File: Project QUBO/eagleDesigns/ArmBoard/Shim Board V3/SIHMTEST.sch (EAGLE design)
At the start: 30 parts, among them IC1 MCP2551/SN, U1 BME280

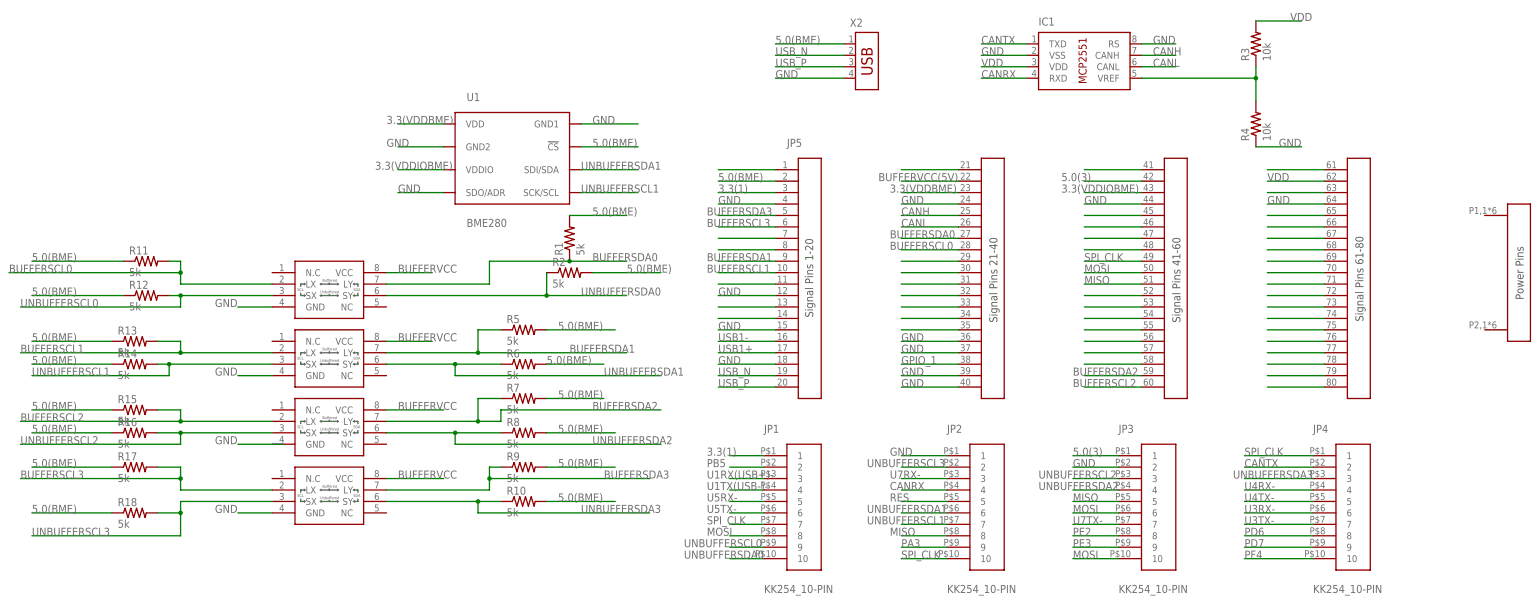
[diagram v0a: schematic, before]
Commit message: 
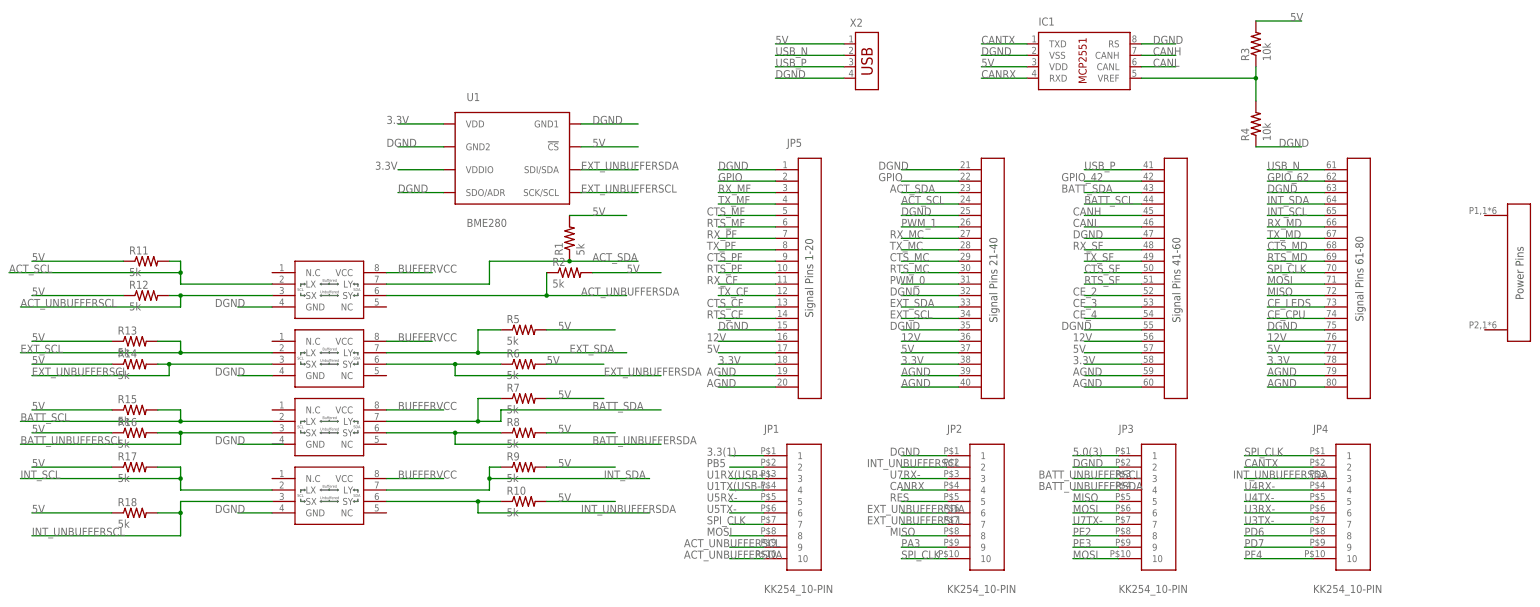
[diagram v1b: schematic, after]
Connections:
- net N$11 renamed RX_CF
- net N$13 renamed CTS_CF
- net N$14 renamed RTS_CF
- net N$29 renamed CTS_MC
- net N$30 renamed RTS_MC
- net N$31 renamed PWM_0
- net N$48 renamed RX_SF
- net N$52 renamed CE_2
- net N$53 renamed CE_3
- net N$54 renamed CE_4
- net N$66 renamed RX_MD
- net N$67 renamed TX_MD
- net N$68 renamed CTS_MD
- net N$69 renamed RTS_MD
- net N$7 renamed RX_PF
- net N$73 renamed CE_LEDS
- net N$74 renamed CE_CPU
- net N$8 renamed TX_PF
- net UNBUFFERSCL0 renamed ACT_UNBUFFERSCL
- net UNBUFFERSCL1 renamed EXT_UNBUFFERSCL
- net UNBUFFERSCL2 renamed BATT_UNBUFFERSCL
- net UNBUFFERSCL3 renamed INT_UNBUFFERSCL
- net UNBUFFERSDA0 renamed ACT_UNBUFFERSDA
- net UNBUFFERSDA1 renamed EXT_UNBUFFERSDA
- net UNBUFFERSDA2 renamed BATT_UNBUFFERSDA
- net UNBUFFERSDA3 renamed INT_UNBUFFERSDA
- removed net 3.3(VDDBME): JP5.P$23, U1.VDD
- removed net 3.3(VDDIOBME): JP5.P$43, U1.VDDIO
- removed net 5.0(BME): JP5.P$2, R1.2, R10.2, R11.1, R12.1, R13.1, R14.1, R15.1, R16.1, R17.1, R18.1, R2.2, R5.2, R6.2, R7.2, R8.2, R9.2, U1.!CS, X2.1
- removed net BUFFERSCL0: JP5.P$28, R11.2, U$1.LX
- removed net BUFFERSCL1: JP5.P$10, R13.2, U$2.LX
- removed net BUFFERSCL2: JP5.P$60, R15.2, U$3.LX
- removed net BUFFERSCL3: JP5.P$6, R17.2, U$4.LX
- removed net BUFFERSDA0: JP5.P$27, R1.1, U$1.LY
- removed net BUFFERSDA1: JP5.P$9, R5.1, U$2.LY
- removed net BUFFERSDA2: JP5.P$59, R7.1, U$3.LY
- removed net BUFFERSDA3: JP5.P$5, R9.1, U$4.LY
- removed net BUFFERVCC(5V): JP5.P$22
- removed net GND: IC1.RS, IC1.VSS, JP2.1, JP3.2, JP5.P$12, JP5.P$15, JP5.P$18, JP5.P$24, JP5.P$36, JP5.P$37, JP5.P$39, JP5.P$4, JP5.P$40, JP5.P$44, JP5.P$64, R4.1, U$1.GND, U$2.GND, U$4.GND, U1.GND1, U1.GND2, U1.SDO/ADR, X2.4
- removed net GPIO_1: JP5.P$38
- removed net N$1: JP5.P$1
- removed net N$21: JP5.P$21
- removed net N$32: JP5.P$32
- removed net N$33: JP5.P$33
- removed net N$34: JP5.P$34
- removed net N$35: JP5.P$35
- removed net N$41: JP5.P$41
- removed net N$45: JP5.P$45
- removed net N$46: JP5.P$46
- removed net N$47: JP5.P$47
- removed net N$55: JP5.P$55
- removed net N$56: JP5.P$56
- removed net N$57: JP5.P$57
- removed net N$58: JP5.P$58
- removed net N$61: JP5.P$61
- removed net N$63: JP5.P$63
- removed net N$65: JP5.P$65
- removed net N$70: JP5.P$70
- removed net N$71: JP5.P$71
- removed net N$72: JP5.P$72
- removed net N$75: JP5.P$75
- removed net N$76: JP5.P$76
- removed net N$77: JP5.P$77
- removed net N$78: JP5.P$78
- removed net N$79: JP5.P$79
- removed net N$80: JP5.P$80
- removed net USB1+: JP5.P$17
- removed net USB1-: JP5.P$16
- removed net VDD: IC1.VDD, JP5.P$62, R3.2
- new net 12V: JP5.P$16, JP5.P$36, JP5.P$56, JP5.P$76
- new net 3.3V: JP5.P$18, JP5.P$38, JP5.P$58, JP5.P$78, U1.VDD, U1.VDDIO
- new net 5V: IC1.VDD, JP5.P$17, JP5.P$37, JP5.P$57, JP5.P$77, R1.2, R10.2, R11.1, R12.1, R13.1, R14.1, R15.1, R16.1, R17.1, R18.1, R2.2, R3.2, R5.2, R6.2, R7.2, R8.2, R9.2, U1.!CS, X2.1
- new net ACT_SCL: JP5.P$24, R11.2, U$1.LX
- new net ACT_SDA: JP5.P$23, R1.1, U$1.LY
- new net AGND: JP5.P$19, JP5.P$20, JP5.P$39, JP5.P$40, JP5.P$59, JP5.P$60, JP5.P$79, JP5.P$80
- new net BATT_SCL: JP5.P$44, R15.2, U$3.LX
- new net BATT_SDA: JP5.P$43, R7.1, U$3.LY
- new net CTS_MF: JP5.P$5
- new net CTS_PF: JP5.P$9
- new net CTS_SF: JP5.P$50
- new net DGND: IC1.RS, IC1.VSS, JP2.1, JP3.2, JP5.P$1, JP5.P$15, JP5.P$21, JP5.P$25, JP5.P$32, JP5.P$35, JP5.P$47, JP5.P$55, JP5.P$63, JP5.P$75, R4.1, U$1.GND, U$2.GND, U$4.GND, U1.GND1, U1.GND2, U1.SDO/ADR, X2.4
- new net EXT_SCL: JP5.P$34, R13.2, U$2.LX
- new net EXT_SDA: JP5.P$33, R5.1, U$2.LY
- new net GPIO: JP5.P$2, JP5.P$22
- new net GPIO_42: JP5.P$42
- new net GPIO_62: JP5.P$62
- new net INT_SCL: JP5.P$65, R17.2, U$4.LX
- new net INT_SDA: JP5.P$64, R9.1, U$4.LY
- new net PWM_1: JP5.P$26
- new net RTS_MF: JP5.P$6
- new net RTS_PF: JP5.P$10
- new net RTS_SF: JP5.P$51
- new net RX_MC: JP5.P$27
- new net RX_MF: JP5.P$3
- new net TX_CF: JP5.P$12
- new net TX_MC: JP5.P$28
- new net TX_MF: JP5.P$4
- new net TX_SF: JP5.P$49
- net 3.3(1): no longer JP5.P$3
- net 5.0(3): no longer JP5.P$42
- net CANH: now also JP5.P$45; no longer JP5.P$25
- net CANL: now also JP5.P$46; no longer JP5.P$26
- net MISO: now also JP5.P$72; no longer JP5.P$51
- net MOSI: now also JP5.P$71; no longer JP5.P$50
- net SPI_CLK: now also JP5.P$70; no longer JP5.P$49
- net USB_N: now also JP5.P$61; no longer JP5.P$19
- net USB_P: now also JP5.P$41; no longer JP5.P$20

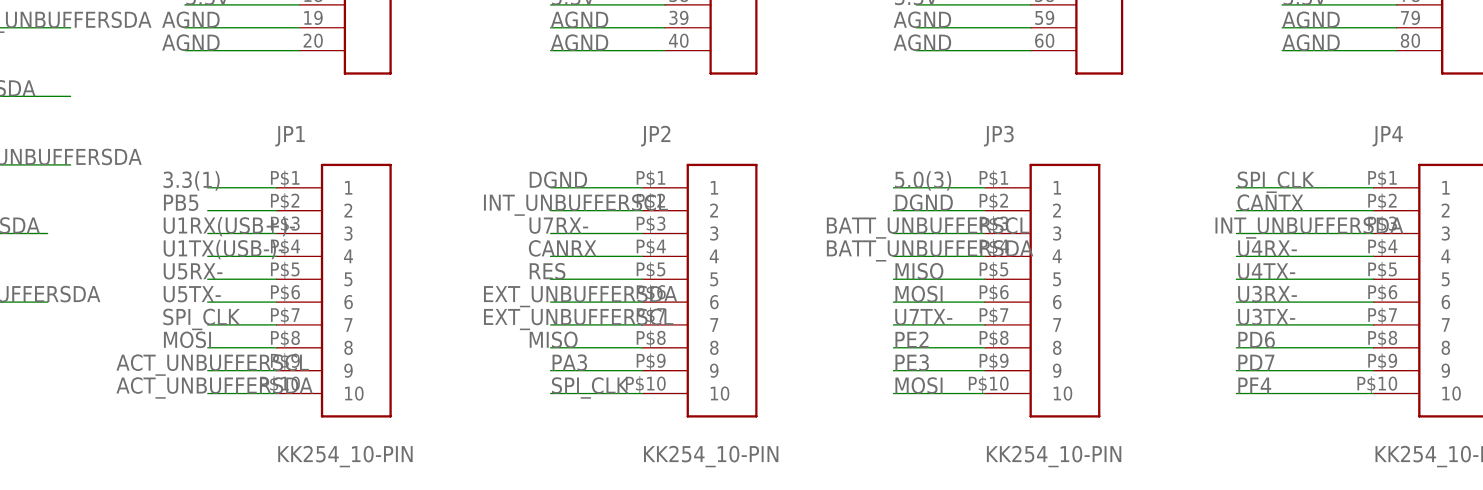
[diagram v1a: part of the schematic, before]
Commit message: 
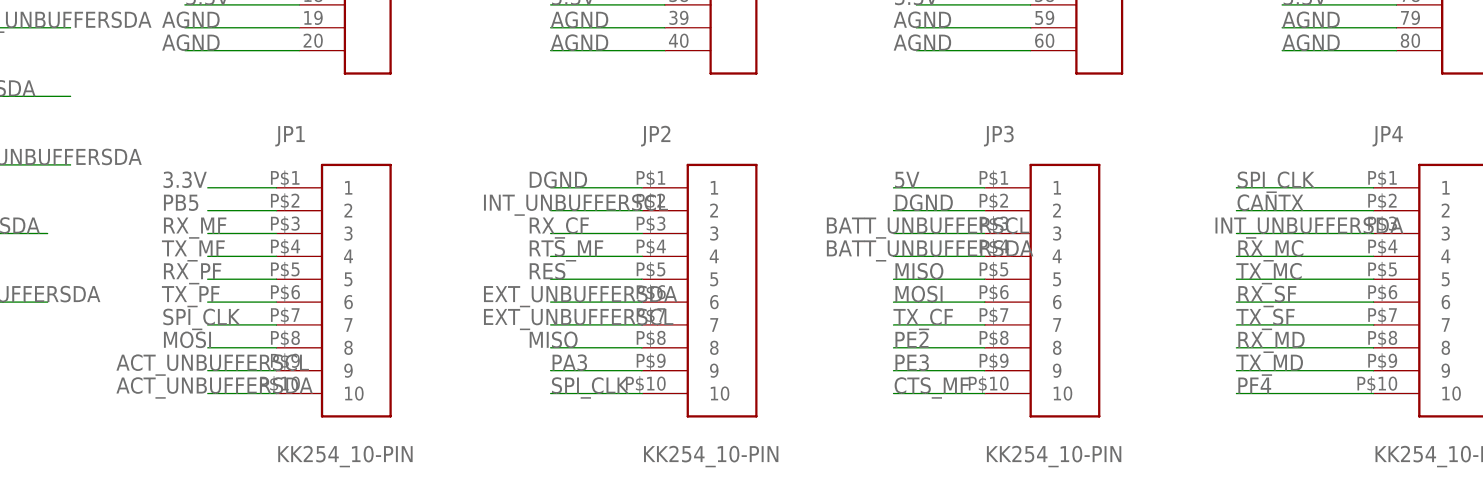
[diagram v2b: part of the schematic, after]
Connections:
- removed net 3.3(1): JP1.1
- removed net 5.0(3): JP3.1
- removed net PD6: JP4.8
- removed net PD7: JP4.9
- removed net U1RX(USB+)-: JP1.3
- removed net U1TX(USB-)-: JP1.4
- removed net U3RX-: JP4.6
- removed net U3TX-: JP4.7
- removed net U4RX-: JP4.4
- removed net U4TX-: JP4.5
- removed net U5RX-: JP1.5
- removed net U5TX-: JP1.6
- removed net U7RX-: JP2.3
- removed net U7TX-: JP3.7
- net 3.3V: now also JP1.1
- net 5V: now also JP3.1
- net CANRX: no longer JP2.4
- net CTS_MF: now also JP3.10
- net MOSI: no longer JP3.10
- net RTS_MF: now also JP2.4
- net RX_CF: now also JP2.3
- net RX_MC: now also JP4.4
- net RX_MD: now also JP4.8
- net RX_MF: now also JP1.3
- net RX_PF: now also JP1.5
- net RX_SF: now also JP4.6
- net TX_CF: now also JP3.7
- net TX_MC: now also JP4.5
- net TX_MD: now also JP4.9
- net TX_MF: now also JP1.4
- net TX_PF: now also JP1.6
- net TX_SF: now also JP4.7
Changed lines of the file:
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@@
 <?xml version="1.0" encoding="utf-8"?>
 <!DOCTYPE eagle SYSTEM "eagle.dtd">
-<eagle version="7.6.0">
+<eagle version="8.0.0">
 <drawing>
 <settings>
@@
 </segment>
 </net>
-<net name="3.3(1)" class="0">
-<segment>
-<pinref part="JP1" gate="G$1" pin="1"/>
-<wire x1="10.16" y1="88.9" x2="2.54" y2="88.9" width="0.1524" layer="91"/>
-<label x="-2.54" y="88.9" size="1.778" layer="95"/>
-</segment>
-</net>
 <net name="RES" class="0">
 <segment>
@@
 </segment>
 </net>
-<net name="5.0(3)" class="0">
-<segment>
-<pinref part="JP3" gate="G$1" pin="1"/>
-<wire x1="88.9" y1="88.9" x2="78.74" y2="88.9" width="0.1524" layer="91"/>
-<label x="78.74" y="88.9" size="1.778" layer="95"/>
-</segment>
-</net>
 <net name="PE2" class="0">
 <segment>
@@
 <wire x1="68.58" y1="180.34" x2="58.42" y2="180.34" width="0.1524" layer="91"/>
 <label x="58.42" y="180.34" size="1.778" layer="95"/>
-</segment>
-</net>
-<net name="PD6" class="0">
-<segment>
-<pinref part="JP4" gate="G$1" pin="8"/>
-<wire x1="132.08" y1="71.12" x2="116.84" y2="71.12" width="0.1524" layer="91"/>
-<label x="116.84" y="71.12" size="1.778" layer="95"/>
-</segment>
-</net>
-<net name="PD7" class="0">
-<segment>
-<pinref part="JP4" gate="G$1" pin="9"/>
-<wire x1="132.08" y1="68.58" x2="116.84" y2="68.58" width="0.1524" layer="91"/>
-<label x="116.84" y="68.58" size="1.778" layer="95"/>
 </segment>
 </net>
@@
 </segment>
 </net>
-<net name="U1RX(USB+)-" class="0">
-<segment>
-<pinref part="JP1" gate="G$1" pin="3"/>
-<wire x1="10.16" y1="83.82" x2="2.54" y2="83.82" width="0.1524" layer="91"/>
-<label x="-2.54" y="83.82" size="1.778" layer="95"/>
-</segment>
-</net>
-<net name="U1TX(USB-)-" class="0">
-<segment>
-<pinref part="JP1" gate="G$1" pin="4"/>
-<wire x1="10.16" y1="81.28" x2="2.54" y2="81.28" width="0.1524" layer="91"/>
-<label x="-2.54" y="81.28" size="1.778" layer="95"/>
-</segment>
-</net>
-<net name="U5RX-" class="0">
-<segment>
-<pinref part="JP1" gate="G$1" pin="5"/>
-<wire x1="10.16" y1="78.74" x2="2.54" y2="78.74" width="0.1524" layer="91"/>
-<label x="-2.54" y="78.74" size="1.778" layer="95"/>
-</segment>
-</net>
-<net name="U5TX-" class="0">
-<segment>
-<pinref part="JP1" gate="G$1" pin="6"/>
-<wire x1="10.16" y1="76.2" x2="2.54" y2="76.2" width="0.1524" layer="91"/>
-<label x="-2.54" y="76.2" size="1.778" layer="95"/>
-</segment>
-</net>
-<net name="U7RX-" class="0">
-<segment>
-<pinref part="JP2" gate="G$1" pin="3"/>
-<wire x1="50.8" y1="83.82" x2="40.64" y2="83.82" width="0.1524" layer="91"/>
-<label x="38.1" y="83.82" size="1.778" layer="95"/>
-</segment>
-</net>
-<net name="U7TX-" class="0">
-<segment>
-<pinref part="JP3" gate="G$1" pin="7"/>
-<wire x1="88.9" y1="73.66" x2="78.74" y2="73.66" width="0.1524" layer="91"/>
-<label x="78.74" y="73.66" size="1.778" layer="95"/>
-</segment>
-</net>
-<net name="U4RX-" class="0">
-<segment>
-<pinref part="JP4" gate="G$1" pin="4"/>
-<wire x1="132.08" y1="81.28" x2="116.84" y2="81.28" width="0.1524" layer="91"/>
-<label x="116.84" y="81.28" size="1.778" layer="95"/>
-</segment>
-</net>
-<net name="U4TX-" class="0">
-<segment>
-<pinref part="JP4" gate="G$1" pin="5"/>
-<wire x1="132.08" y1="78.74" x2="116.84" y2="78.74" width="0.1524" layer="91"/>
-<label x="116.84" y="78.74" size="1.778" layer="95"/>
-</segment>
-</net>
-<net name="U3RX-" class="0">
-<segment>
-<pinref part="JP4" gate="G$1" pin="6"/>
-<wire x1="132.08" y1="76.2" x2="116.84" y2="76.2" width="0.1524" layer="91"/>
-<label x="116.84" y="76.2" size="1.778" layer="95"/>
-</segment>
-</net>
-<net name="U3TX-" class="0">
-<segment>
-<pinref part="JP4" gate="G$1" pin="7"/>
-<wire x1="132.08" y1="73.66" x2="116.84" y2="73.66" width="0.1524" layer="91"/>
-<label x="116.84" y="73.66" size="1.778" layer="95"/>
-</segment>
-</net>
 <net name="ACT_UNBUFFERSCL" class="0">
 <segment>
@@
 </segment>
 <segment>
-<pinref part="JP3" gate="G$1" pin="10"/>
-<wire x1="88.9" y1="66.04" x2="78.74" y2="66.04" width="0.1524" layer="91"/>
-<label x="78.74" y="66.04" size="1.778" layer="95"/>
-</segment>
-<segment>
 <pinref part="JP5" gate="G$1" pin="P$71"/>
 <wire x1="134.62" y1="127" x2="121.92" y2="127" width="0.1524" layer="91"/>
@@
 <label x="-2.54" y="137.16" size="1.778" layer="95"/>
 </segment>
+<segment>
+<pinref part="JP1" gate="G$1" pin="5"/>
+<wire x1="10.16" y1="78.74" x2="2.54" y2="78.74" width="0.1524" layer="91"/>
+<label x="-2.54" y="78.74" size="1.778" layer="95"/>
+</segment>
 </net>
 <net name="TX_PF" class="0">
@@
 <label x="-2.54" y="134.62" size="1.778" layer="95"/>
 </segment>
+<segment>
+<pinref part="JP1" gate="G$1" pin="6"/>
+<wire x1="10.16" y1="76.2" x2="2.54" y2="76.2" width="0.1524" layer="91"/>
+<label x="-2.54" y="76.2" size="1.778" layer="95"/>
+</segment>
 </net>
 <net name="RX_CF" class="0">
@@
 <wire x1="12.7" y1="127" x2="0" y2="127" width="0.1524" layer="91"/>
 <label x="-2.54" y="127" size="1.778" layer="95"/>
+</segment>
+<segment>
+<pinref part="JP2" gate="G$1" pin="3"/>
+<wire x1="50.8" y1="83.82" x2="40.64" y2="83.82" width="0.1524" layer="91"/>
+<label x="38.1" y="83.82" size="1.778" layer="95"/>
 </segment>
 </net>
@@
 <wire x1="93.98" y1="134.62" x2="81.28" y2="134.62" width="0.1524" layer="91"/>
 <label x="78.74" y="134.62" size="1.778" layer="95"/>
+</segment>
+<segment>
+<pinref part="JP4" gate="G$1" pin="6"/>
+<wire x1="132.08" y1="76.2" x2="116.84" y2="76.2" width="0.1524" layer="91"/>
+<label x="116.84" y="76.2" size="1.778" layer="95"/>
 </segment>
 </net>
@@
 <label x="121.92" y="139.7" size="1.778" layer="95"/>
 </segment>
+<segment>
+<pinref part="JP4" gate="G$1" pin="8"/>
+<wire x1="132.08" y1="71.12" x2="116.84" y2="71.12" width="0.1524" layer="91"/>
+<label x="116.84" y="71.12" size="1.778" layer="95"/>
+</segment>
 </net>
 <net name="TX_MD" class="0">
@@
 <label x="121.92" y="137.16" size="1.778" layer="95"/>
 </segment>
+<segment>
+<pinref part="JP4" gate="G$1" pin="9"/>
+<wire x1="132.08" y1="68.58" x2="116.84" y2="68.58" width="0.1524" layer="91"/>
+<label x="116.84" y="68.58" size="1.778" layer="95"/>
+</segment>
 </net>
 <net name="CTS_MD" class="0">
@@
 </net>
 <net name="CANRX" class="0">
-<segment>
-<pinref part="JP2" gate="G$1" pin="4"/>
-<wire x1="50.8" y1="81.28" x2="40.64" y2="81.28" width="0.1524" layer="91"/>
-<label x="38.1" y="81.28" size="1.778" layer="95"/>
-</segment>
 <segment>
 <pinref part="IC1" gate="X" pin="RXD"/>
@@
 <label x="0" y="147.32" size="1.778" layer="95"/>
 </segment>
+<segment>
+<pinref part="JP1" gate="G$1" pin="3"/>
+<wire x1="10.16" y1="83.82" x2="2.54" y2="83.82" width="0.1524" layer="91"/>
+<label x="-2.54" y="83.82" size="1.778" layer="95"/>
+</segment>
 </net>
 <net name="TX_MF" class="0">
@@
 <label x="0" y="144.78" size="1.778" layer="95"/>
 </segment>
+<segment>
+<pinref part="JP1" gate="G$1" pin="4"/>
+<wire x1="10.16" y1="81.28" x2="2.54" y2="81.28" width="0.1524" layer="91"/>
+<label x="-2.54" y="81.28" size="1.778" layer="95"/>
+</segment>
 </net>
 <net name="CTS_MF" class="0">
@@
 <label x="-2.54" y="142.24" size="1.778" layer="95"/>
 </segment>
+<segment>
+<pinref part="JP3" gate="G$1" pin="10"/>
+<wire x1="88.9" y1="66.04" x2="78.74" y2="66.04" width="0.1524" layer="91"/>
+<label x="78.74" y="66.04" size="1.778" layer="95"/>
+</segment>
 </net>
 <net name="RTS_MF" class="0">
@@
 <label x="-2.54" y="139.7" size="1.778" layer="95"/>
 </segment>
+<segment>
+<pinref part="JP2" gate="G$1" pin="4"/>
+<wire x1="50.8" y1="81.28" x2="40.64" y2="81.28" width="0.1524" layer="91"/>
+<label x="38.1" y="81.28" size="1.778" layer="95"/>
+</segment>
 </net>
 <net name="12V" class="0">
@@
 <label x="-152.4" y="76.2" size="1.778" layer="95"/>
 </segment>
+<segment>
+<pinref part="JP3" gate="G$1" pin="1"/>
+<wire x1="88.9" y1="88.9" x2="78.74" y2="88.9" width="0.1524" layer="91"/>
+<label x="78.74" y="88.9" size="1.778" layer="95"/>
+</segment>
 </net>
 <net name="AGND" class="0">
@@
 <label x="0" y="124.46" size="1.778" layer="95"/>
 </segment>
+<segment>
+<pinref part="JP3" gate="G$1" pin="7"/>
+<wire x1="88.9" y1="73.66" x2="78.74" y2="73.66" width="0.1524" layer="91"/>
+<label x="78.74" y="73.66" size="1.778" layer="95"/>
+</segment>
 </net>
 <net name="3.3V" class="0">
@@
 <wire x1="-60.96" y1="152.4" x2="-71.12" y2="152.4" width="0.1524" layer="91"/>
 <label x="-76.2" y="152.4" size="1.778" layer="95"/>
+</segment>
+<segment>
+<pinref part="JP1" gate="G$1" pin="1"/>
+<wire x1="10.16" y1="88.9" x2="2.54" y2="88.9" width="0.1524" layer="91"/>
+<label x="-2.54" y="88.9" size="1.778" layer="95"/>
 </segment>
 </net>
@@
 <label x="38.1" y="137.16" size="1.778" layer="95"/>
 </segment>
+<segment>
+<pinref part="JP4" gate="G$1" pin="4"/>
+<wire x1="132.08" y1="81.28" x2="116.84" y2="81.28" width="0.1524" layer="91"/>
+<label x="116.84" y="81.28" size="1.778" layer="95"/>
+</segment>
 </net>
 <net name="TX_MC" class="0">
@@
 <wire x1="53.34" y1="134.62" x2="40.64" y2="134.62" width="0.1524" layer="91"/>
 <label x="38.1" y="134.62" size="1.778" layer="95"/>
+</segment>
+<segment>
+<pinref part="JP4" gate="G$1" pin="5"/>
+<wire x1="132.08" y1="78.74" x2="116.84" y2="78.74" width="0.1524" layer="91"/>
+<label x="116.84" y="78.74" size="1.778" layer="95"/>
 </segment>
 </net>
@@
 <label x="81.28" y="132.08" size="1.778" layer="95"/>
 </segment>
-</net>
+<segment>
+<pinref part="JP4" gate="G$1" pin="7"/>
+<wire x1="132.08" y1="73.66" x2="116.84" y2="73.66" width="0.1524" layer="91"/>
+<label x="116.84" y="73.66" size="1.778" layer="95"/>
+</segment>
+</net>
